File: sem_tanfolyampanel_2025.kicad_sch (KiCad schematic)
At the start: 29 parts, among them J1 USB_C_Receptacle_USB2.0_16P, J2 Conn_01x09, J3 Conn_01x09, SW1 RESET, U1 STM32F030F4Px, U2 LD1117S33TR_SOT223, U3 CH32V203G6U6

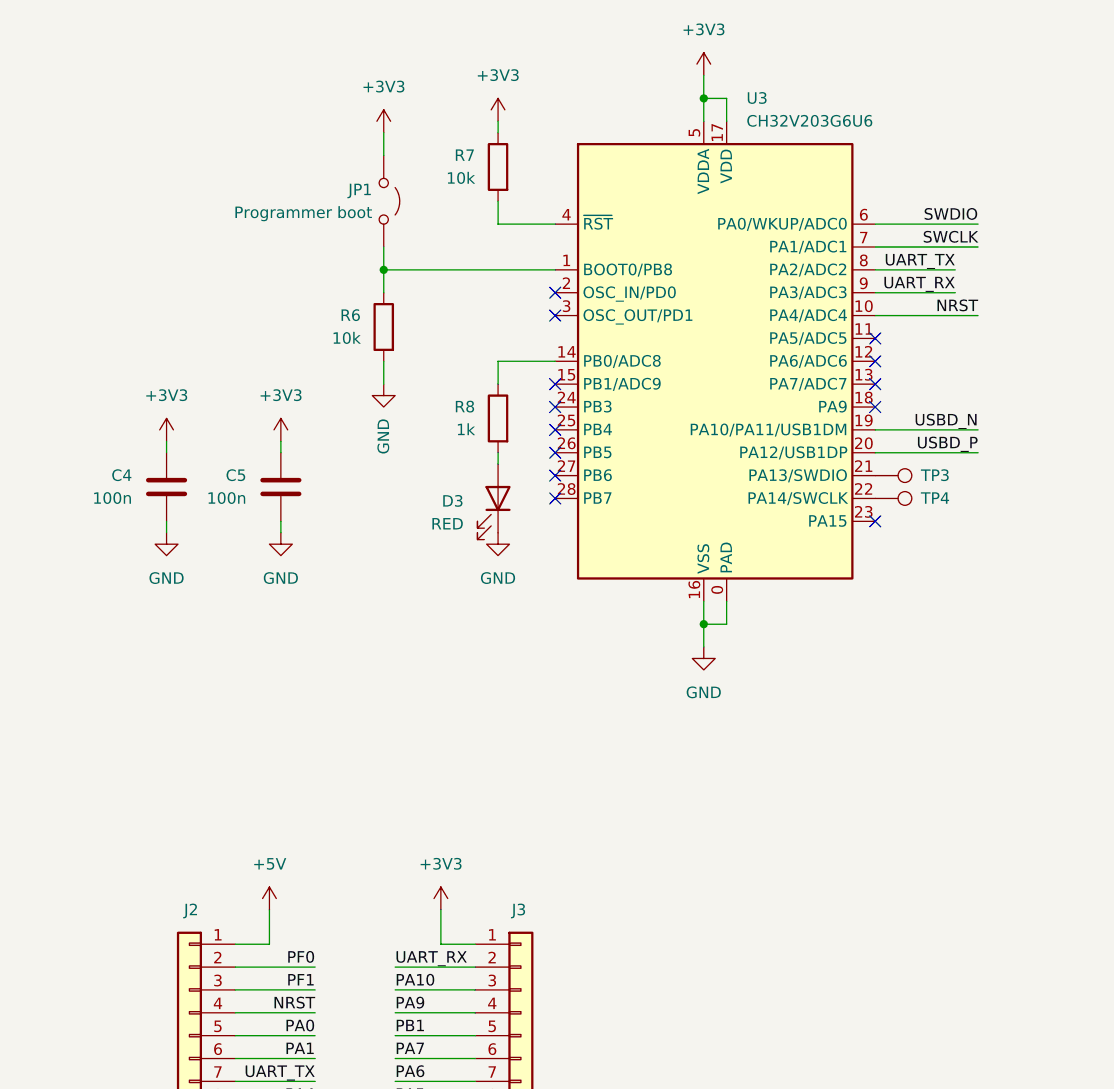
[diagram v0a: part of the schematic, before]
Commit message: First iteration of PCB routing
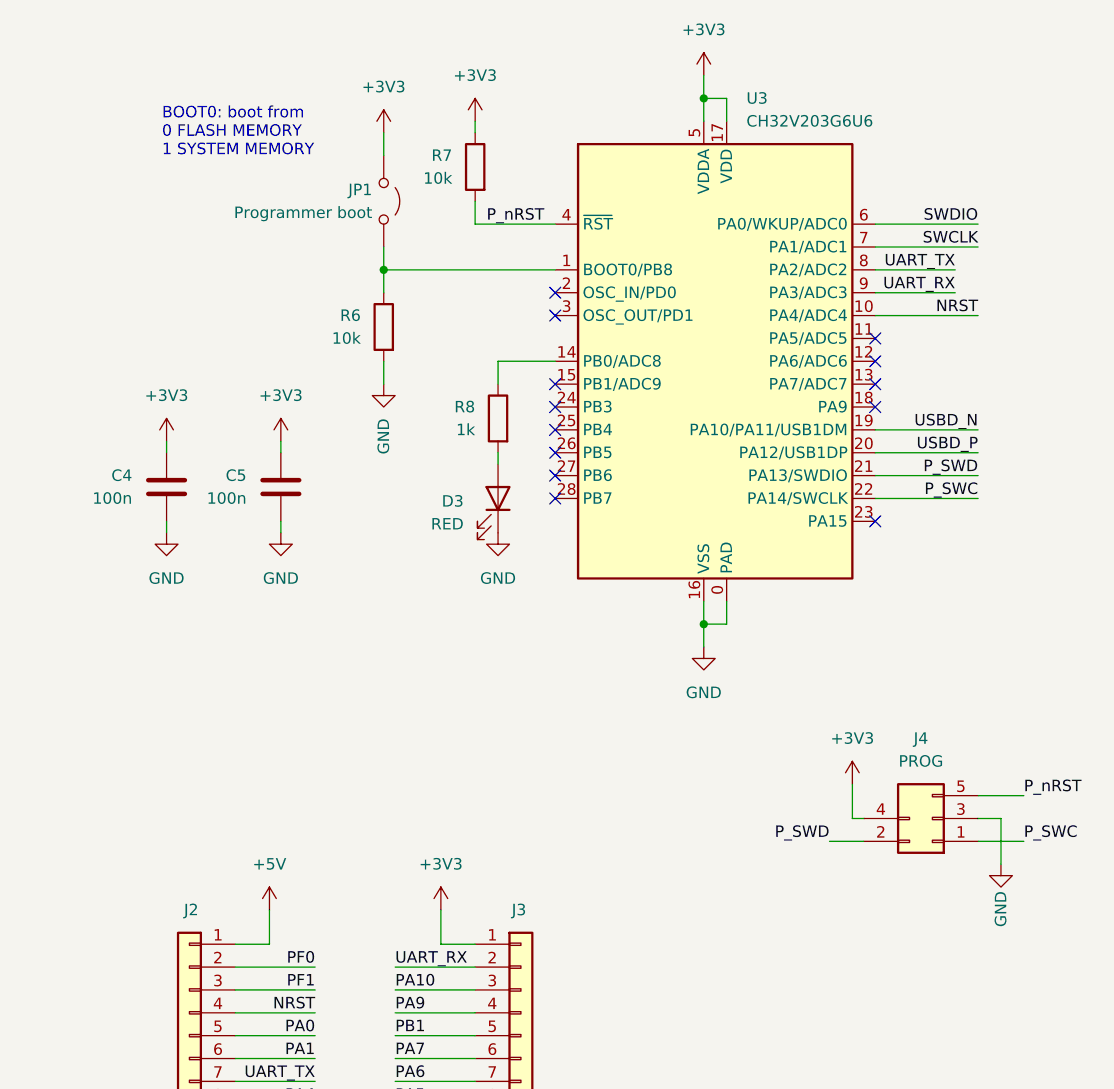
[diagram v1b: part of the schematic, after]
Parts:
- removed TP3, TP4: TestPoint, TestPoint:TestPoint_Pad_D1.0mm, symbol Connector:TestPoint
- added J4: PROG, jlcpcb:ProgConnector_5pin, symbol Connector_Generic:Conn_2Rows-05Pins
- JP1: footprint Connector_PinHeader_2.54mm:PinHeader_2x01_P2.54mm_Vertical -> Jumper:SolderJumper-2_P1.3mm_Open_TrianglePad1.0x1.5mm
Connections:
- net +3V3: now also J4.4 (Pin_4)
- net GND: now also J4.3 (Pin_3)
- net P_SWC: now reaches U3.22 (PA14/SWCLK)
- net P_SWC: now also J4.1 (Pin_1)
- net P_SWD: now reaches U3.21 (PA13/SWDIO)
- net P_SWD: now also J4.2 (Pin_2)
- net P_nRST: now reaches R7.2, U3.4 (~{RST})
- net P_nRST: now also J4.5 (Pin_5)
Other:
- note added: "BOOT0: boot from 0 FLASH MEMORY 1 SYSTEM MEMORY"
- moved on the sheet: R7

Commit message: Rerouting and finalizing.
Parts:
- removed TP1, TP2: TestPoint, TestPoint:TestPoint_Pad_D1.0mm, symbol Connector:TestPoint
- C1, C3: footprint Capacitor_SMD:C_0603_1608Metric -> Capacitor_SMD:C_0805_2012Metric
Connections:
- net GND: now also U3.29 (PAD); no longer U3.0 (PAD)
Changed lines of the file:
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@@
 			)
 		)
-		(property "Description" ""
+		(property "Description" "Generic connector, double row, 05 pins, odd/even pin numbering scheme (row 1 odd numbers, row 2 even numbers), script generated (kicad-library-utils/schlib/autogen/connector/)"
 			(at 260.35 114.3 0)
 			(effects
@@
 			)
 		)
-		(property "Footprint" "Capacitor_SMD:C_0603_1608Metric"
+		(property "Footprint" "Capacitor_SMD:C_0805_2012Metric"
 			(at 116.5352 60.96 0)
 			(effects
@@
 		)
 		(instances
-			(project ""
+			(project "sem_tanfolyampanel_2025"
 				(path "/3ef41fba-c582-47d1-87c6-b4f77528e269"
 					(reference "C1")
@@
 	)
 	(symbol
-		(lib_id "Connector:TestPoint")
-		(at 64.77 78.74 270)
-		(unit 1)
-		(exclude_from_sim no)
-		(in_bom yes)
-		(on_board yes)
-		(dnp no)
-		(property "Reference" "TP1"
-			(at 69.85 78.74 90)
-			(effects
-				(font
-					(size 1.27 1.27)
-				)
-				(justify left)
-			)
-		)
-		(property "Value" "TestPoint"
-			(at 69.85 80.0099 90)
-			(effects
-				(font
-					(size 1.27 1.27)
-				)
-				(justify left)
-				(hide yes)
-			)
-		)
-		(property "Footprint" "TestPoint:TestPoint_Pad_D1.0mm"
-			(at 64.77 83.82 0)
-			(effects
-				(font
-					(size 1.27 1.27)
-				)
-				(hide yes)
-			)
-		)
-		(property "Datasheet" "~"
-			(at 64.77 83.82 0)
-			(effects
-				(font
-					(size 1.27 1.27)
-				)
-				(hide yes)
-			)
-		)
-		(property "Description" "test point"
-			(at 64.77 78.74 0)
-			(effects
-				(font
-					(size 1.27 1.27)
-				)
-				(hide yes)
-			)
-		)
-		(pin "1"
-		)
-		(instances
-			(project ""
-				(path "/3ef41fba-c582-47d1-87c6-b4f77528e269"
-					(reference "TP1")
-					(unit 1)
-				)
-			)
-		)
-	)
-	(symbol
 		(lib_id "power:GND")
 		(at 205.74 152.4 0)
@@
 		)
 		(instances
-			(project ""
+			(project "sem_tanfolyampanel_2025"
 				(path "/3ef41fba-c582-47d1-87c6-b4f77528e269"
 					(reference "#PWR07")
@@
 		)
 		(instances
-			(project ""
+			(project "sem_tanfolyampanel_2025"
 				(path "/3ef41fba-c582-47d1-87c6-b4f77528e269"
 					(reference "F1")
@@
 		)
 		(instances
-			(project ""
+			(project "sem_tanfolyampanel_2025"
 				(path "/3ef41fba-c582-47d1-87c6-b4f77528e269"
 					(reference "JP1")
@@
 		)
 		(instances
-			(project ""
-				(path "/3ef41fba-c582-47d1-87c6-b4f77528e269"
-					(reference "#PWR015")
-					(unit 1)
-				)
-			)
-		)
-	)
-	(symbol
-		(lib_id "Connector:TestPoint")
-		(at 64.77 81.28 270)
-		(unit 1)
-		(exclude_from_sim no)
-		(in_bom yes)
-		(on_board yes)
-		(dnp no)
-		(property "Reference" "TP2"
-			(at 69.85 81.28 90)
-			(effects
-				(font
-					(size 1.27 1.27)
-				)
-				(justify left)
-			)
-		)
-		(property "Value" "TestPoint"
-			(at 69.85 82.5499 90)
-			(effects
-				(font
-					(size 1.27 1.27)
-				)
-				(justify left)
-				(hide yes)
-			)
-		)
-		(property "Footprint" "TestPoint:TestPoint_Pad_D1.0mm"
-			(at 64.77 86.36 0)
-			(effects
-				(font
-					(size 1.27 1.27)
-				)
-				(hide yes)
-			)
-		)
-		(property "Datasheet" "~"
-			(at 64.77 86.36 0)
-			(effects
-				(font
-					(size 1.27 1.27)
-				)
-				(hide yes)
-			)
-		)
-		(property "Description" "test point"
-			(at 64.77 81.28 0)
-			(effects
-				(font
-					(size 1.27 1.27)
-				)
-				(hide yes)
-			)
-		)
-		(pin "1"
-		)
-		(instances
 			(project "sem_tanfolyampanel_2025"
 				(path "/3ef41fba-c582-47d1-87c6-b4f77528e269"
-					(reference "TP2")
+					(reference "#PWR015")
 					(unit 1)
 				)
@@
 		)
 		(instances
-			(project ""
+			(project "sem_tanfolyampanel_2025"
 				(path "/3ef41fba-c582-47d1-87c6-b4f77528e269"
 					(reference "C2")
@@
 		)
 		(instances
-			(project ""
+			(project "sem_tanfolyampanel_2025"
 				(path "/3ef41fba-c582-47d1-87c6-b4f77528e269"
 					(reference "J3")
@@
 		)
 		(instances
-			(project ""
+			(project "sem_tanfolyampanel_2025"
 				(path "/3ef41fba-c582-47d1-87c6-b4f77528e269"
 					(reference "R1")
@@
 		(pin "7"
 		)
-		(pin "0"
+		(pin "29"
 		)
 		(pin "28"
@@
 		)
 		(instances
-			(project ""
+			(project "sem_tanfolyampanel_2025"
 				(path "/3ef41fba-c582-47d1-87c6-b4f77528e269"
 					(reference "U3")
@@
 			)
 		)
-		(property "Description" ""
+		(property "Description" "Power symbol creates a global label with name \"GND\" , ground"
 			(at 267.97 119.38 0)
 			(effects
@@
 		)
 		(instances
-			(project ""
+			(project "sem_tanfolyampanel_2025"
 				(path "/3ef41fba-c582-47d1-87c6-b4f77528e269"
 					(reference "R3")
@@
 		)
 		(instances
-			(project ""
+			(project "sem_tanfolyampanel_2025"
 				(path "/3ef41fba-c582-47d1-87c6-b4f77528e269"
 					(reference "U1")
@@
 		)
 		(instances
-			(project ""
+			(project "sem_tanfolyampanel_2025"
 				(path "/3ef41fba-c582-47d1-87c6-b4f77528e269"
 					(reference "#FLG01")
@@
 		)
 		(instances
-			(project ""
+			(project "sem_tanfolyampanel_2025"
 				(path "/3ef41fba-c582-47d1-87c6-b4f77528e269"
 					(reference "D1")
@@
 		)
 		(instances
-			(project ""
+			(project "sem_tanfolyampanel_2025"
 				(path "/3ef41fba-c582-47d1-87c6-b4f77528e269"
 					(reference "U2")
@@
 		)
 		(instances
-			(project ""
+			(project "sem_tanfolyampanel_2025"
 				(path "/3ef41fba-c582-47d1-87c6-b4f77528e269"
 					(reference "#PWR03")
@@
 		)
 		(instances
-			(project ""
+			(project "sem_tanfolyampanel_2025"
 				(path "/3ef41fba-c582-47d1-87c6-b4f77528e269"
 					(reference "J1")
@@
 	)
 	(symbol
-		(lib_id "Device:C")
-		(at 147.32 57.15 0)
-		(unit 1)
-		(exclude_from_sim no)
-		(in_bom yes)
-		(on_board yes)
-		(dnp no)
-		(fields_autoplaced yes)
-		(property "Reference" "C3"
-			(at 151.13 55.8799 0)
-			(effects
-				(font
-					(size 1.27 1.27)
-				)
-				(justify left)
-			)
-		)
-		(property "Value" "10u"
-			(at 151.13 58.4199 0)
-			(effects
-				(font
-					(size 1.27 1.27)
-				)
-				(justify left)
-			)
-		)
-		(property "Footprint" "Capacitor_SMD:C_0603_1608Metric"
-			(at 148.2852 60.96 0)
-			(effects
-				(font
-					(size 1.27 1.27)
-				)
-				(hide yes)
-			)
-		)
-		(property "Datasheet" "~"
-			(at 147.32 57.15 0)
-			(effects
-				(font
-					(size 1.27 1.27)
-				)
-				(hide yes)
-			)
-		)
-		(property "Description" "Unpolarized capacitor"
-			(at 147.32 57.15 0)
-			(effects
-				(font
-					(size 1.27 1.27)
-				)
-				(hide yes)
-			)
-		)
-		(pin "1"
-		)
-		(pin "2"
-		)
-		(instances
-			(project "sem_tanfolyampanel_2025"
-				(path "/3ef41fba-c582-47d1-87c6-b4f77528e269"
-					(reference "C3")
-					(unit 1)
-				)
-			)
-		)
-	)
-	(symbol
 		(lib_id "power:+5V")
 		(at 115.57 46.99 0)
@@
 		)
 		(instances
-			(project ""
+			(project "sem_tanfolyampanel_2025"
 				(path "/3ef41fba-c582-47d1-87c6-b4f77528e269"
 					(reference "#PWR09")
@@
 		)
 		(instances
-			(project ""
+			(project "sem_tanfolyampanel_2025"
 				(path "/3ef41fba-c582-47d1-87c6-b4f77528e269"
 					(reference "SW1")
@@
 					(unit 1)
 				)
+			)
+		)
+	)
+	(symbol
+		(lib_id "Device:C")
+		(at 147.32 57.15 0)
+		(unit 1)
+		(exclude_from_sim no)
+		(in_bom yes)
+		(on_board yes)
+		(dnp no)
+		(fields_autoplaced yes)
+		(property "Reference" "C3"
+			(at 151.13 55.8799 0)
+			(effects
+				(font
+					(size 1.27 1.27)
+				)
+				(justify left)
+			)
+		)
+		(property "Value" "10u"
+			(at 151.13 58.4199 0)
+			(effects
+				(font
+					(size 1.27 1.27)
+				)
+				(justify left)
+			)
+		)
+		(property "Footprint" "Capacitor_SMD:C_0805_2012Metric"
+			(at 148.2852 60.96 0)
+			(effects
+				(font
+					(size 1.27 1.27)
+				)
+				(hide yes)
+			)
+		)
+		(property "Datasheet" "~"
+			(at 147.32 57.15 0)
+			(effects
+				(font
+					(size 1.27 1.27)
+				)
+				(hide yes)
+			)
+		)
+		(property "Description" "Unpolarized capacitor"
+			(at 147.32 57.15 0)
+			(effects
+				(font
+					(size 1.27 1.27)
+				)
+				(hide yes)
+			)
+		)
+		(pin "1"
+		)
+		(pin "2"
+		)
+		(instances
+			(project "sem_tanfolyampanel_2025"
+				(path "/3ef41fba-c582-47d1-87c6-b4f77528e269"
+					(reference "C3")
+					(unit 1)
+				)
